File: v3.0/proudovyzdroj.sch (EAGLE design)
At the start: 26 parts, among them IC1 LM358N, IC2 LM358N, Q1 IRF512

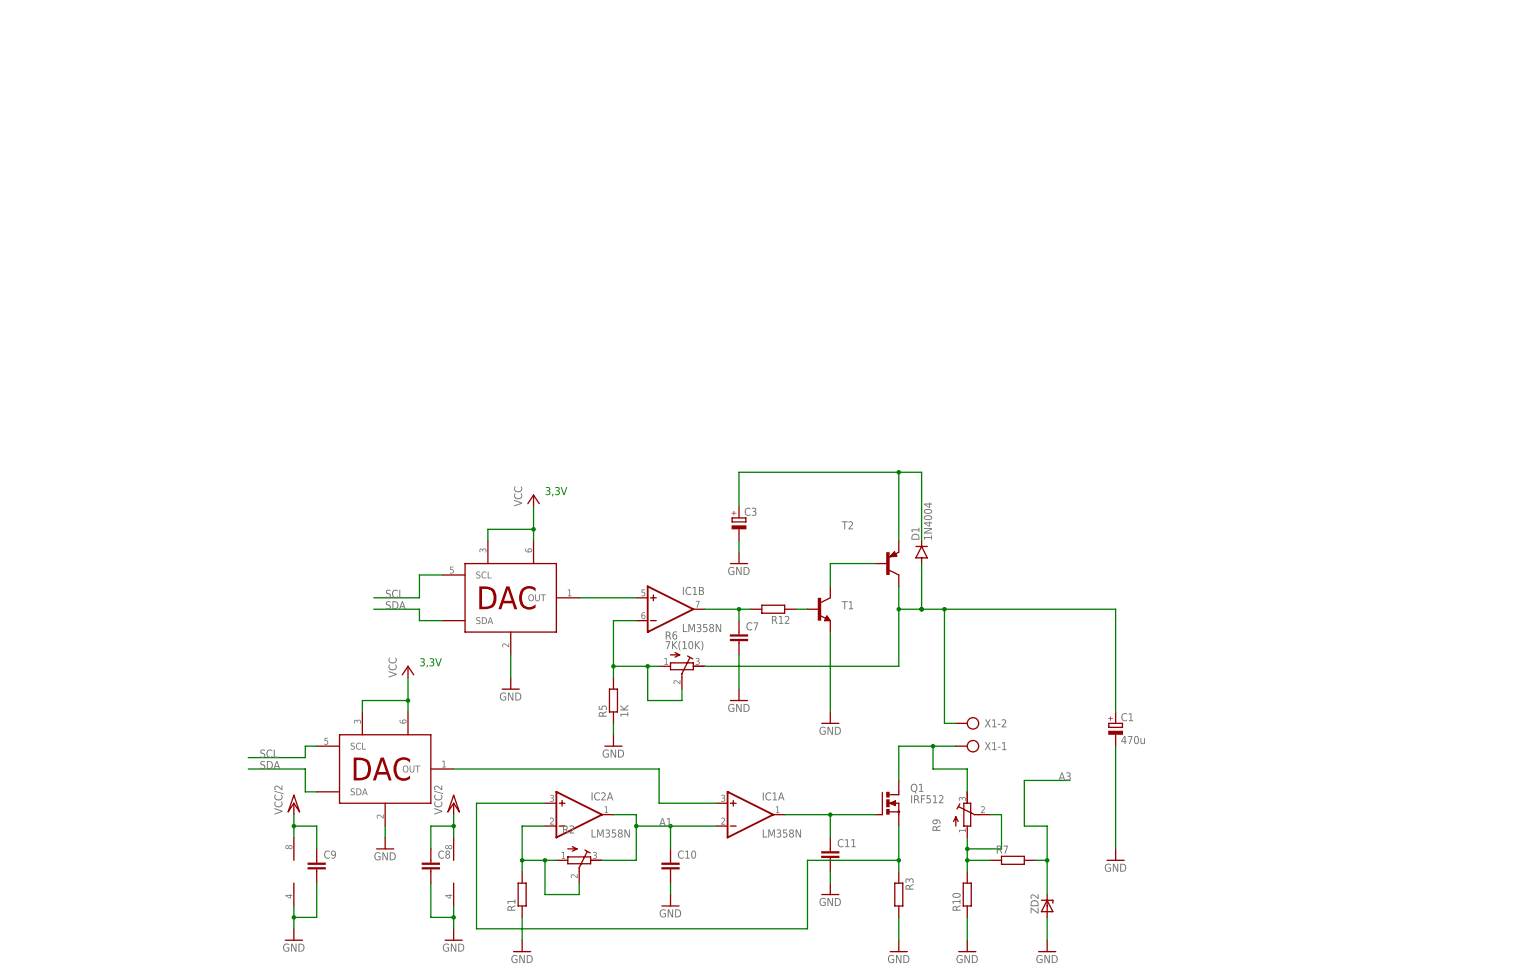
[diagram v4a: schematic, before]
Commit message: přidána rozlévaná měď, rozšířena dokumentace
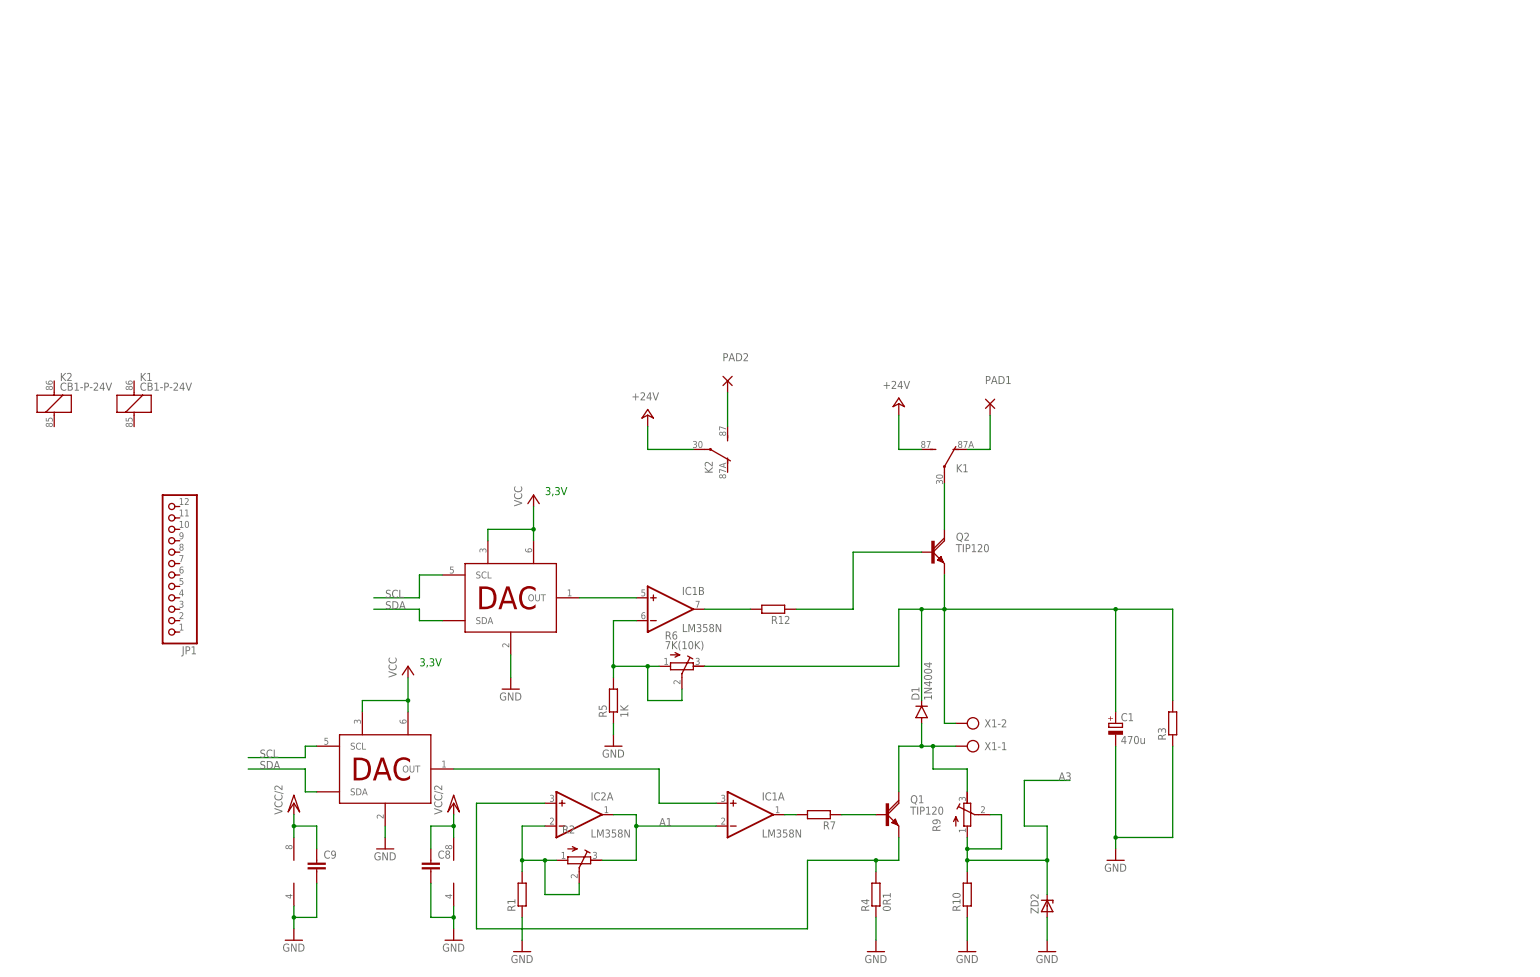
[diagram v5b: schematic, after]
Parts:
- removed C10, C11, C7: (no value), rcl:C-EUC0805
- removed C3: (no value), rcl:CPOL-EUE3.5-8
- removed T1: (no value), transistor:BC337-40-NPN-TO92-CBE
- removed T2: (no value), transistor-neu-to92:-PNP-TO220V
- added JP1: (no value), pinhead:PINHD-1X12
- added K1, K2: CB1-P-24V, relay:CB1-P-24V
- added PAD1, PAD2: (no value), wirepad:3,81/1,4
- added Q2: TIP120, transistor-power:TIP120
- added R4: 0R1, rcl:R-EU_0411/15
- Q1: value IRF512 -> TIP120; device transistor-power:IRF512 -> transistor-power:TIP120
- R3: device rcl:R-EU_0207/10 -> rcl:R-EU_R0805
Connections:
- removed net N$24: C3.+, D1.C, T2.E
- new net +24V: K12.S, K22.P
- new net N$10: K12.O, PAD1.P
- new net N$14: K22.S, PAD2.P
- net A1: no longer C10.1
- net A3: now also R10.2, R9.A, R9.S; no longer R7.2
- net GND: now also R3.1, R4.1; no longer C10.2, C11.2, C3.-, C7.2, R3.2, T1.E
- net N$1: now also Q1.E, R4.2; no longer Q1.S, R3.1
- net N$12: no longer C7.1
- net N$13: now also D1.C, Q2.E, R3.2; no longer D1.A, T2.C
- net N$2: now also R7.2; no longer C11.1, Q1.G
- net N$4: now also Q2.B; no longer T1.B
- net N$5: now also Q1.B; no longer R10.2, R9.A, R9.S
- net N$7: now also D1.A, Q1.C; no longer Q1.D
- net N$8: now also K12.P, Q2.C; no longer T1.C, T2.B
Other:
- moved on the sheet: D1, R3, R7

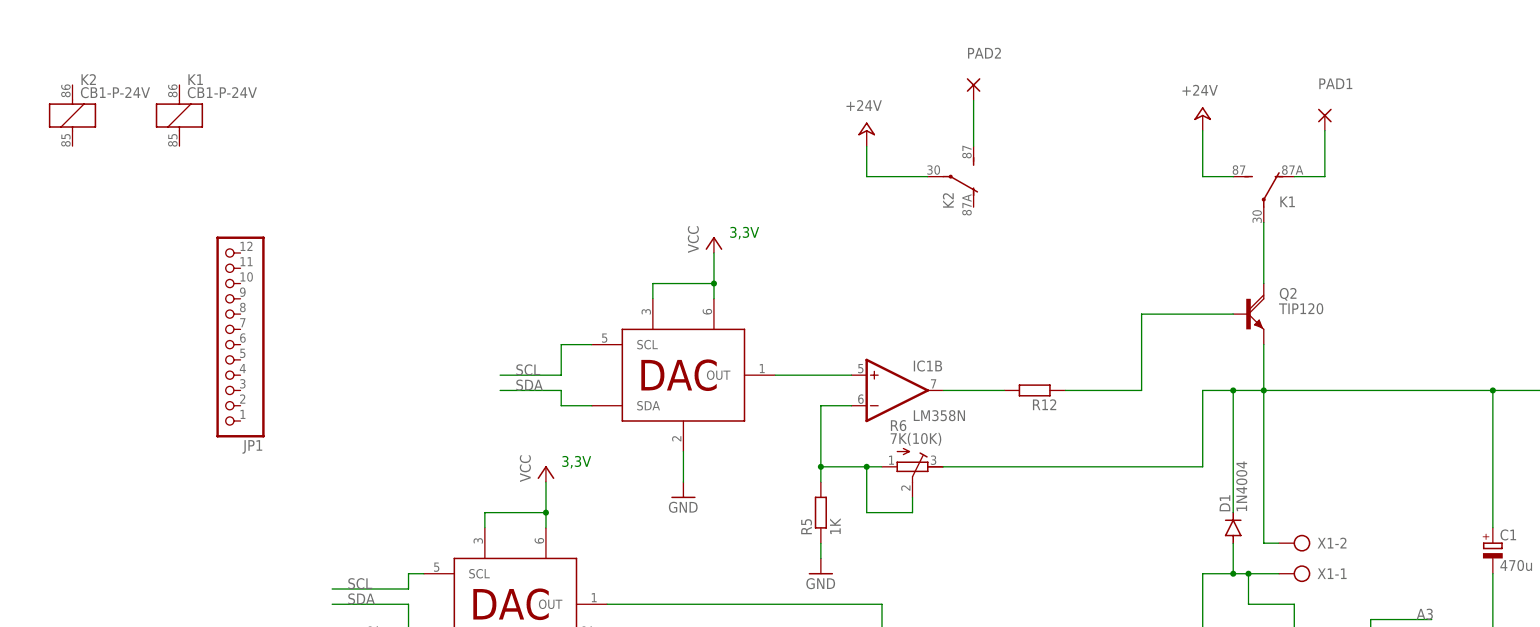
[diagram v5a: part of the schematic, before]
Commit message: Přidán obvod řízení výběru zdroje lineárního regulátoru
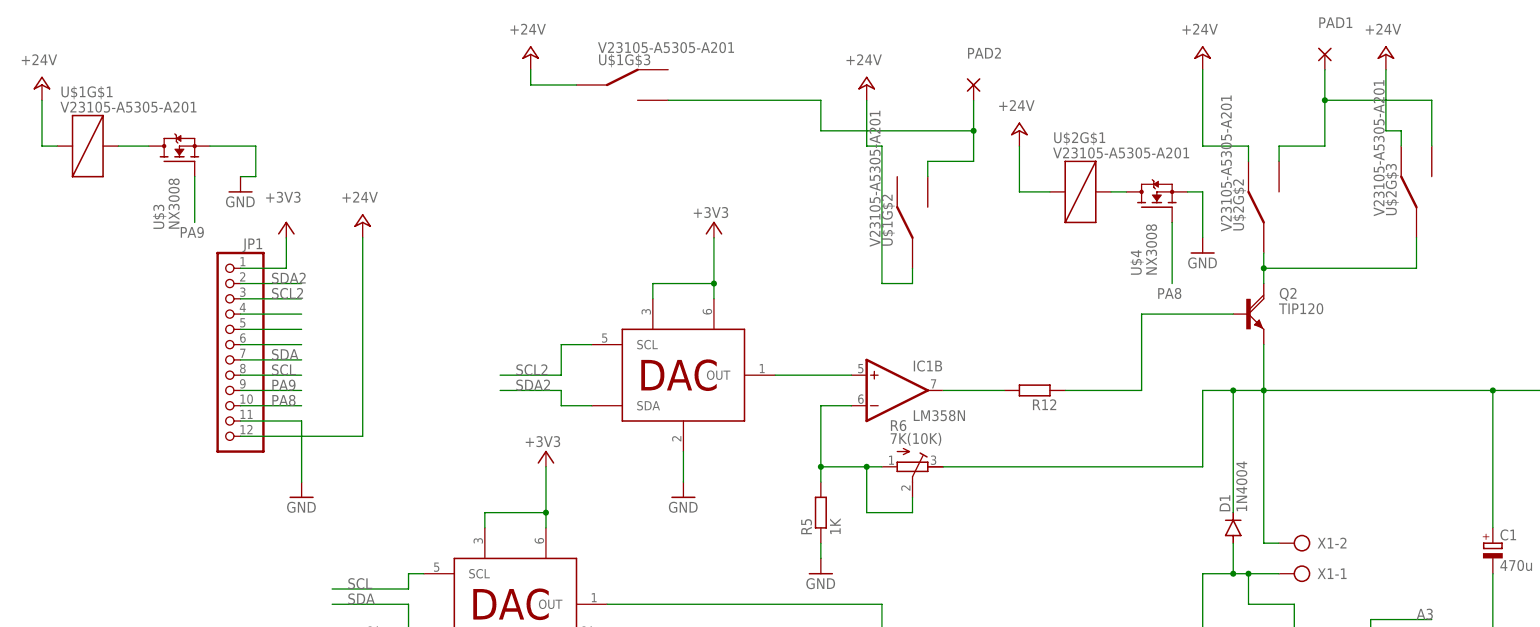
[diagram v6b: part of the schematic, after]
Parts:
- removed K1, K2: CB1-P-24V, relay:CB1-P-24V
- added U$1, U$2: V23105-A5305-A201, realatka:V23105-A5305-A201
- added U$3, U$4: NX3008, NEXPERIA :NX3008
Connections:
- removed net VCC: U$5.VDD, U$5.VREF, U$6.VDD, U$6.VREF
- new net +3V3: JP1.1, U$5.VDD, U$5.VREF, U$6.VDD, U$6.VREF
- new net N$15: JP1.5
- new net N$16: U$1G$1.C$2, U$3.D
- new net N$17: U$2G$1.C$2, U$4.D
- new net N$18: JP1.6
- new net N$19: PAD2.P, U$1G$2.3, U$1G$3.3
- new net PA8: JP1.10, U$4.G
- new net PA9: JP1.9, U$3.G
- new net SCL2: JP1.3, U$6.SCL
- new net SDA2: JP1.2, U$6.SDA
- net +24V: now also JP1.12, U$1G$1.C$1, U$1G$2.1, U$1G$3.1, U$2G$1.C$1, U$2G$2.2, U$2G$3.2; no longer K12.S, K22.P
- net GND: now also JP1.11, U$3.S, U$4.S
- net N$10: now also U$2G$2.3, U$2G$3.3; no longer K12.O
- net N$14: now also JP1.4; no longer K22.S, PAD2.P
- net N$8: now also U$2G$2.1, U$2G$3.1; no longer K12.P
- net SCL: now also JP1.8; no longer U$6.SCL
- net SDA: now also JP1.7; no longer U$6.SDA
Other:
- note removed: "3,3V"
- moved on the sheet: JP1, PAD1
